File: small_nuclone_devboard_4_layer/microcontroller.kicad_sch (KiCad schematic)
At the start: 1 part

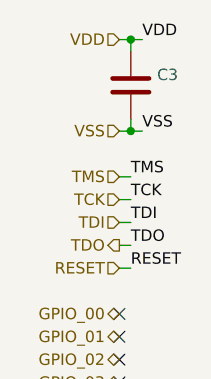
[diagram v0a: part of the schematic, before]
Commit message: updated 4 layer nuclone template
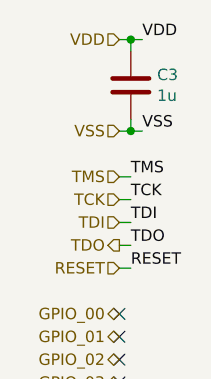
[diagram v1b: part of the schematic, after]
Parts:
- C3: value (none) -> 1u; footprint (none) -> SquantorRcl:C_0402
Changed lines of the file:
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@@
       (effects (font (size 1.27 1.27)) (justify left))
     )
-    (property "Value" "" (id 1) (at 28.321 29.083 0)
+    (property "Value" "1u" (id 1) (at 28.321 29.083 0)
       (effects (font (size 1.27 1.27)) (justify left))
     )
-    (property "Footprint" "" (id 2) (at 26.3652 31.75 0)
+    (property "Footprint" "SquantorRcl:C_0402" (id 2) (at 26.3652 31.75 0)
       (effects (font (size 1.27 1.27)) hide)
     )
